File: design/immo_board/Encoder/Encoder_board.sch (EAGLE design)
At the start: 4 parts

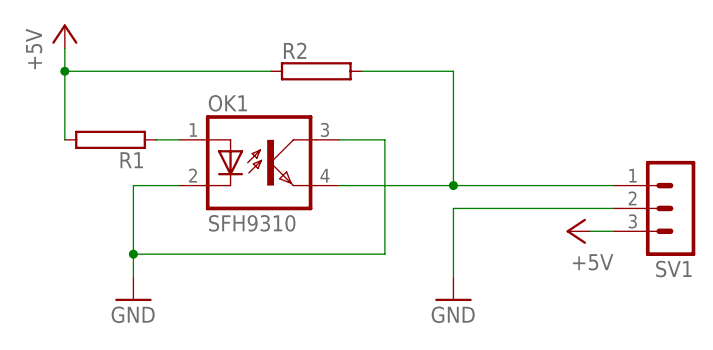
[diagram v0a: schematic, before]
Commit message: Fix board and electric scheme. Add capacitors.
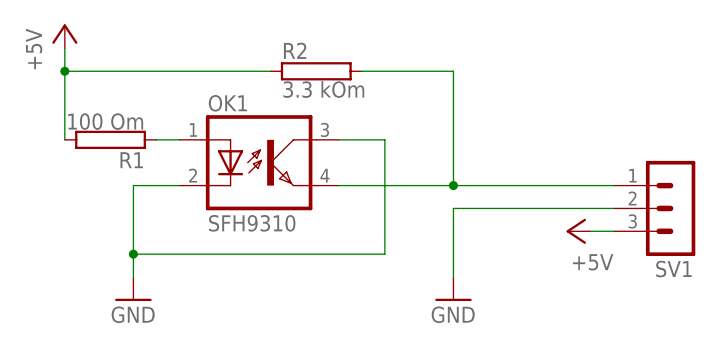
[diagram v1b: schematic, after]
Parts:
- R1: value (none) -> 100 Om
- R2: value (none) -> 3.3 kOm
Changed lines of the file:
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@@
 <parts>
 <part name="OK1" library="optocoupler" deviceset="SFH9*" device="310"/>
-<part name="R1" library="resistor-power" deviceset="R" device="RS1/4"/>
-<part name="R2" library="resistor-power" deviceset="R" device="RS1/4"/>
+<part name="R1" library="resistor-power" deviceset="R" device="RS1/4" value="100 Om"/>
+<part name="R2" library="resistor-power" deviceset="R" device="RS1/4" value="3.3 kOm"/>
 <part name="P+1" library="supply1" deviceset="+5V" device=""/>
 <part name="GND1" library="supply1" deviceset="GND" device=""/>
